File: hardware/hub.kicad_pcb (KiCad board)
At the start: 4 copper layers, 100 x 85 mm, 153 parts, among them J101 USB-A, J102 TNG-Power-BTM, J103 TNG-Power-TOP, J104 TNG-Data-BTM, J105 TNG-Data-TOP, P101 Debug, P102 PE, P202 PWR IN, SW101 BOOT, T201 744272251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

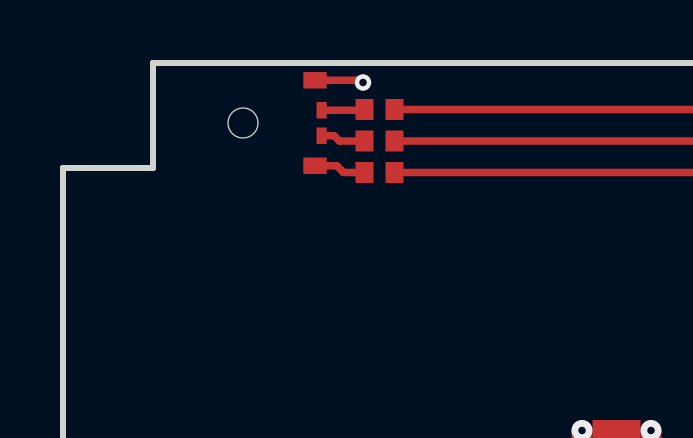
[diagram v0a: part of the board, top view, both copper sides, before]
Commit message: update rgb led drill diameter
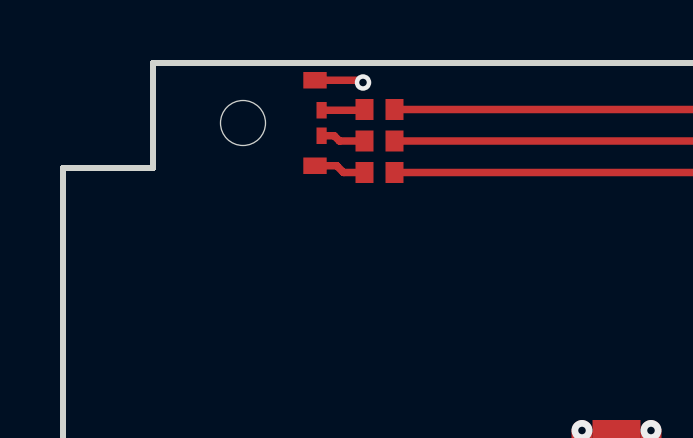
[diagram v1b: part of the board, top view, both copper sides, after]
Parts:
- LED101: footprint LED-RGB-LP -> kicad-libraries:LED-RGB-LP
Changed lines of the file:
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@@
   )
   (setup
-    (last_trace_width 0.5)
+    (last_trace_width 0.15)
     (user_trace_width 0.15)
     (user_trace_width 0.2)
@@
     (add_net STACK_USB_D4_F-)
   )
+  (module kicad-libraries:LED-RGB-LP (layer F.Cu)
+    (at 65.85 52.95 90)
+    (fp_text reference LED101 (at 0 0 90) (layer F.Fab)
+      (effects (font (size 0.15 0.15) (thickness 0.0375)))
+    )
+    (fp_text value EASV3015RGBA0 (at 0 -0.3 90) (layer F.Fab)
+      (effects (font (size 0.15 0.15) (thickness 0.0375)))
+    )
+    (fp_line (start -1 -1.4) (end 1 -1.4) (layer F.Fab) (width 0.1))
+    (fp_line (start 1 -1.4) (end 1 -8.4) (layer F.Fab) (width 0.1))
+    (fp_line (start 1 -8.4) (end -1 -8.4) (layer F.Fab) (width 0.1))
+    (fp_line (start -1 -8.4) (end -1 -1.4) (layer F.Fab) (width 0.1))
+    (fp_line (start -1.5 -0.5) (end -1.5 0.2) (layer F.Fab) (width 0.025))
+    (fp_line (start 1.5 -0.5) (end -1.5 -0.5) (layer F.Fab) (width 0.025))
+    (fp_line (start 1.5 0.2) (end 1.5 -0.5) (layer F.Fab) (width 0.025))
+    (fp_line (start -1.5 0.2) (end 1.5 0.2) (layer F.Fab) (width 0.025))
+    (fp_arc (start 0 -0.5) (end -0.8 -0.5) (angle 90) (layer F.Fab) (width 0.025))
+    (fp_arc (start 0 -0.5) (end 0 -1.3) (angle 90) (layer F.Fab) (width 0.025))
+    (pad 3 smd rect (at -0.425 0.22 90) (size 0.55 0.34) (layers F.Cu F.Paste F.Mask)
+      (net 30 "Net-(LED101-Pad3)"))
+    (pad 2 smd rect (at 0.425 0.22 90) (size 0.55 0.34) (layers F.Cu F.Paste F.Mask)
+      (net 29 "Net-(LED101-Pad2)"))
+    (pad 4 smd rect (at -1.425 0 90) (size 0.55 0.78) (layers F.Cu F.Paste F.Mask)
+      (net 28 "Net-(LED101-Pad4)"))
+    (pad 1 smd rect (at 1.425 0 90) (size 0.55 0.78) (layers F.Cu F.Paste F.Mask)
+      (net 8 3V3))
+    (pad "" np_thru_hole circle (at 0 -2.4 90) (size 1.5 1.5) (drill 1.5) (layers *.Cu *.Mask))
+  )
   (module WE-LHMI (layer F.Cu)
     (at 97.45 112.0437 90)
@@
     )
   )
-  (module LED-RGB-LP (layer F.Cu)
-    (at 65.85 52.95 90)
-    (fp_text reference LED101 (at 0 0 90) (layer F.Fab)
-      (effects (font (size 0.15 0.15) (thickness 0.0375)))
-    )
-    (fp_text value EASV3015RGBA0 (at 0 -0.3 90) (layer F.Fab)
-      (effects (font (size 0.15 0.15) (thickness 0.0375)))
-    )
-    (fp_arc (start 0 -0.5) (end 0 -1.3) (angle 90) (layer F.Fab) (width 0.025))
-    (fp_arc (start 0 -0.5) (end -0.8 -0.5) (angle 90) (layer F.Fab) (width 0.025))
-    (fp_line (start -1.5 0.2) (end 1.5 0.2) (layer F.Fab) (width 0.025))
-    (fp_line (start 1.5 0.2) (end 1.5 -0.5) (layer F.Fab) (width 0.025))
-    (fp_line (start 1.5 -0.5) (end -1.5 -0.5) (layer F.Fab) (width 0.025))
-    (fp_line (start -1.5 -0.5) (end -1.5 0.2) (layer F.Fab) (width 0.025))
-    (fp_line (start -1 -8.4) (end -1 -1.4) (layer F.Fab) (width 0.1))
-    (fp_line (start 1 -8.4) (end -1 -8.4) (layer F.Fab) (width 0.1))
-    (fp_line (start 1 -1.4) (end 1 -8.4) (layer F.Fab) (width 0.1))
-    (fp_line (start -1 -1.4) (end 1 -1.4) (layer F.Fab) (width 0.1))
-    (pad "" np_thru_hole circle (at 0 -2.4 90) (size 1 1) (drill 1) (layers *.Cu *.Mask))
-    (pad 1 smd rect (at 1.425 0 90) (size 0.55 0.78) (layers F.Cu F.Paste F.Mask)
-      (net 8 3V3))
-    (pad 4 smd rect (at -1.425 0 90) (size 0.55 0.78) (layers F.Cu F.Paste F.Mask)
-      (net 28 "Net-(LED101-Pad4)"))
-    (pad 2 smd rect (at 0.425 0.22 90) (size 0.55 0.34) (layers F.Cu F.Paste F.Mask)
-      (net 29 "Net-(LED101-Pad2)"))
-    (pad 3 smd rect (at -0.425 0.22 90) (size 0.55 0.34) (layers F.Cu F.Paste F.Mask)
-      (net 30 "Net-(LED101-Pad3)"))
-  )
   (module kicad-libraries:DEBUG_PAD (layer F.Cu)

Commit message: fix inductor footprint
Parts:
- LED101: footprint kicad-libraries:LED-RGB-LP -> LED-RGB-LP
- T201: footprint WE-SL5 -> kicad-libraries:WE-SL5
- turned T201 to 0 degrees
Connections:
- T201 pad 1: GND -> Net-(C204-Pad1)
- T201 pad 3: Net-(C204-Pad1) -> GND
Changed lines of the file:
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@@
     (add_net STACK_USB_D4_F-)
   )
-  (module kicad-libraries:LED-RGB-LP (layer F.Cu)
-    (at 65.85 52.95 90)
-    (fp_text reference LED101 (at 0 0 90) (layer F.Fab)
+  (module kicad-libraries:WE-SL5 (layer F.Cu)
+    (at 72.85 128.2437)
+    (fp_text reference T201 (at 0 0.5 180) (layer F.Fab)
       (effects (font (size 0.15 0.15) (thickness 0.0375)))
     )
-    (fp_text value EASV3015RGBA0 (at 0 -0.3 90) (layer F.Fab)
+    (fp_text value 744272251 (at 0 -0.5 180) (layer F.Fab)
       (effects (font (size 0.15 0.15) (thickness 0.0375)))
     )
-    (fp_line (start -1 -1.4) (end 1 -1.4) (layer F.Fab) (width 0.1))
-    (fp_line (start 1 -1.4) (end 1 -8.4) (layer F.Fab) (width 0.1))
-    (fp_line (start 1 -8.4) (end -1 -8.4) (layer F.Fab) (width 0.1))
-    (fp_line (start -1 -8.4) (end -1 -1.4) (layer F.Fab) (width 0.1))
-    (fp_line (start -1.5 -0.5) (end -1.5 0.2) (layer F.Fab) (width 0.025))
-    (fp_line (start 1.5 -0.5) (end -1.5 -0.5) (layer F.Fab) (width 0.025))
-    (fp_line (start 1.5 0.2) (end 1.5 -0.5) (layer F.Fab) (width 0.025))
-    (fp_line (start -1.5 0.2) (end 1.5 0.2) (layer F.Fab) (width 0.025))
-    (fp_arc (start 0 -0.5) (end -0.8 -0.5) (angle 90) (layer F.Fab) (width 0.025))
-    (fp_arc (start 0 -0.5) (end 0 -1.3) (angle 90) (layer F.Fab) (width 0.025))
-    (pad 3 smd rect (at -0.425 0.22 90) (size 0.55 0.34) (layers F.Cu F.Paste F.Mask)
-      (net 30 "Net-(LED101-Pad3)"))
-    (pad 2 smd rect (at 0.425 0.22 90) (size 0.55 0.34) (layers F.Cu F.Paste F.Mask)
-      (net 29 "Net-(LED101-Pad2)"))
-    (pad 4 smd rect (at -1.425 0 90) (size 0.55 0.78) (layers F.Cu F.Paste F.Mask)
-      (net 28 "Net-(LED101-Pad4)"))
-    (pad 1 smd rect (at 1.425 0 90) (size 0.55 0.78) (layers F.Cu F.Paste F.Mask)
-      (net 8 3V3))
-    (pad "" np_thru_hole circle (at 0 -2.4 90) (size 1.5 1.5) (drill 1.5) (layers *.Cu *.Mask))
+    (fp_line (start -5 4.4) (end -5 -4.4) (layer F.Fab) (width 0.1))
+    (fp_line (start 5 4.4) (end -5 4.4) (layer F.Fab) (width 0.1))
+    (fp_line (start 5 -4.4) (end 5 4.4) (layer F.Fab) (width 0.1))
+    (fp_line (start -5 -4.4) (end 5 -4.4) (layer F.Fab) (width 0.1))
+    (fp_circle (center -3.5 -2) (end -3.2 -1.7) (layer F.Fab) (width 0.1))
+    (pad 2 smd rect (at -3.81 3.11) (size 2.7 2.7) (layers F.Cu F.Paste F.Mask)
+      (net 10 "Net-(C204-Pad2)"))
+    (pad 3 smd rect (at 3.81 3.11) (size 2.7 2.7) (layers F.Cu F.Paste F.Mask)
+      (net 67 GND))
+    (pad 4 smd rect (at 3.81 -3.11) (size 2.7 2.7) (layers F.Cu F.Paste F.Mask)
+      (net 14 "Net-(C211-Pad1)"))
+    (pad 1 smd rect (at -3.81 -3.11) (size 2.7 2.7) (layers F.Cu F.Paste F.Mask)
+      (net 9 "Net-(C204-Pad1)"))
+    (model ${KICAD_SYMBOL_DIR}/3d/Inductors/WE-SL5.wrl
+      (at (xyz 0 0 0))
+      (scale (xyz 1 1 1))
+      (rotate (xyz 0 0 0))
+    )
   )
   (module WE-LHMI (layer F.Cu)
@@
     )
   )
-  (module WE-SL5 (layer F.Cu)
-    (at 72.85 128.2437 180)
-    (attr smd)
-    (fp_text reference T201 (at 0 0.5 180) (layer F.Fab)
-      (effects (font (size 0.15 0.15) (thickness 0.0375)))
-    )
-    (fp_text value 744272251 (at 0 -0.5 180) (layer F.Fab)
-      (effects (font (size 0.15 0.15) (thickness 0.0375)))
-    )
-    (fp_circle (center -3.5 1.5) (end -3.2 1.8) (layer F.Fab) (width 0.1))
-    (fp_line (start -5 -4.4) (end 5 -4.4) (layer F.Fab) (width 0.1))
-    (fp_line (start 5 -4.4) (end 5 4.4) (layer F.Fab) (width 0.1))
-    (fp_line (start 5 4.4) (end -5 4.4) (layer F.Fab) (width 0.1))
-    (fp_line (start -5 4.4) (end -5 -4.4) (layer F.Fab) (width 0.1))
-    (pad 1 smd rect (at -3.81 -3.11 180) (size 2.7 2.7) (layers F.Cu F.Paste F.Mask)
-      (net 67 GND))
-    (pad 2 smd rect (at 3.81 -3.11 180) (size 2.7 2.7) (layers F.Cu F.Paste F.Mask)
-      (net 10 "Net-(C204-Pad2)"))
-    (pad 3 smd rect (at 3.81 3.11 180) (size 2.7 2.7) (layers F.Cu F.Paste F.Mask)
-      (net 9 "Net-(C204-Pad1)"))
-    (pad 4 smd rect (at -3.81 3.11 180) (size 2.7 2.7) (layers F.Cu F.Paste F.Mask)
-      (net 14 "Net-(C211-Pad1)"))
-    (model Inductors/WE-SL5.wrl
-      (at (xyz 0 0 0))
-      (scale (xyz 1 1 1))
-      (rotate (xyz 0 0 0))
-    )
-  )
   (module C0402F (layer F.Cu)
     (at 79.45 104.5437 180)
@@
     )
   )
+  (module LED-RGB-LP (layer F.Cu)
+    (at 65.85 52.95 90)
+    (fp_text reference LED101 (at 0 0 90) (layer F.Fab)
+      (effects (font (size 0.15 0.15) (thickness 0.0375)))
+    )
+    (fp_text value EASV3015RGBA0 (at 0 -0.3 90) (layer F.Fab)
+      (effects (font (size 0.15 0.15) (thickness 0.0375)))
+    )
+    (fp_arc (start 0 -0.5) (end 0 -1.3) (angle 90) (layer F.Fab) (width 0.025))
+    (fp_arc (start 0 -0.5) (end -0.8 -0.5) (angle 90) (layer F.Fab) (width 0.025))
+    (fp_line (start -1.5 0.2) (end 1.5 0.2) (layer F.Fab) (width 0.025))
+    (fp_line (start 1.5 0.2) (end 1.5 -0.5) (layer F.Fab) (width 0.025))
+    (fp_line (start 1.5 -0.5) (end -1.5 -0.5) (layer F.Fab) (width 0.025))
+    (fp_line (start -1.5 -0.5) (end -1.5 0.2) (layer F.Fab) (width 0.025))
+    (fp_line (start -1 -8.4) (end -1 -1.4) (layer F.Fab) (width 0.1))
+    (fp_line (start 1 -8.4) (end -1 -8.4) (layer F.Fab) (width 0.1))
+    (fp_line (start 1 -1.4) (end 1 -8.4) (layer F.Fab) (width 0.1))
+    (fp_line (start -1 -1.4) (end 1 -1.4) (layer F.Fab) (width 0.1))
+    (pad "" np_thru_hole circle (at 0 -2.4 90) (size 1.5 1.5) (drill 1.5) (layers *.Cu *.Mask))
+    (pad 1 smd rect (at 1.425 0 90) (size 0.55 0.78) (layers F.Cu F.Paste F.Mask)
+      (net 8 3V3))
+    (pad 4 smd rect (at -1.425 0 90) (size 0.55 0.78) (layers F.Cu F.Paste F.Mask)
+      (net 28 "Net-(LED101-Pad4)"))
+    (pad 2 smd rect (at 0.425 0.22 90) (size 0.55 0.34) (layers F.Cu F.Paste F.Mask)
+      (net 29 "Net-(LED101-Pad2)"))
+    (pad 3 smd rect (at -0.425 0.22 90) (size 0.55 0.34) (layers F.Cu F.Paste F.Mask)
+      (net 30 "Net-(LED101-Pad3)"))
+  )
   (gr_line (start 57.45 80) (end 57.45 135.95) (layer Edge.Cuts) (width 0.2))
